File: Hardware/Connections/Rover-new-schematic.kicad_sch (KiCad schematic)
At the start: 7 parts, among them J1 Motor_Forward_Right, J2 motor_forward_left, J3 motor_back_left, J4 motor_back_right, U1 ESP32-DEVKIT-V1

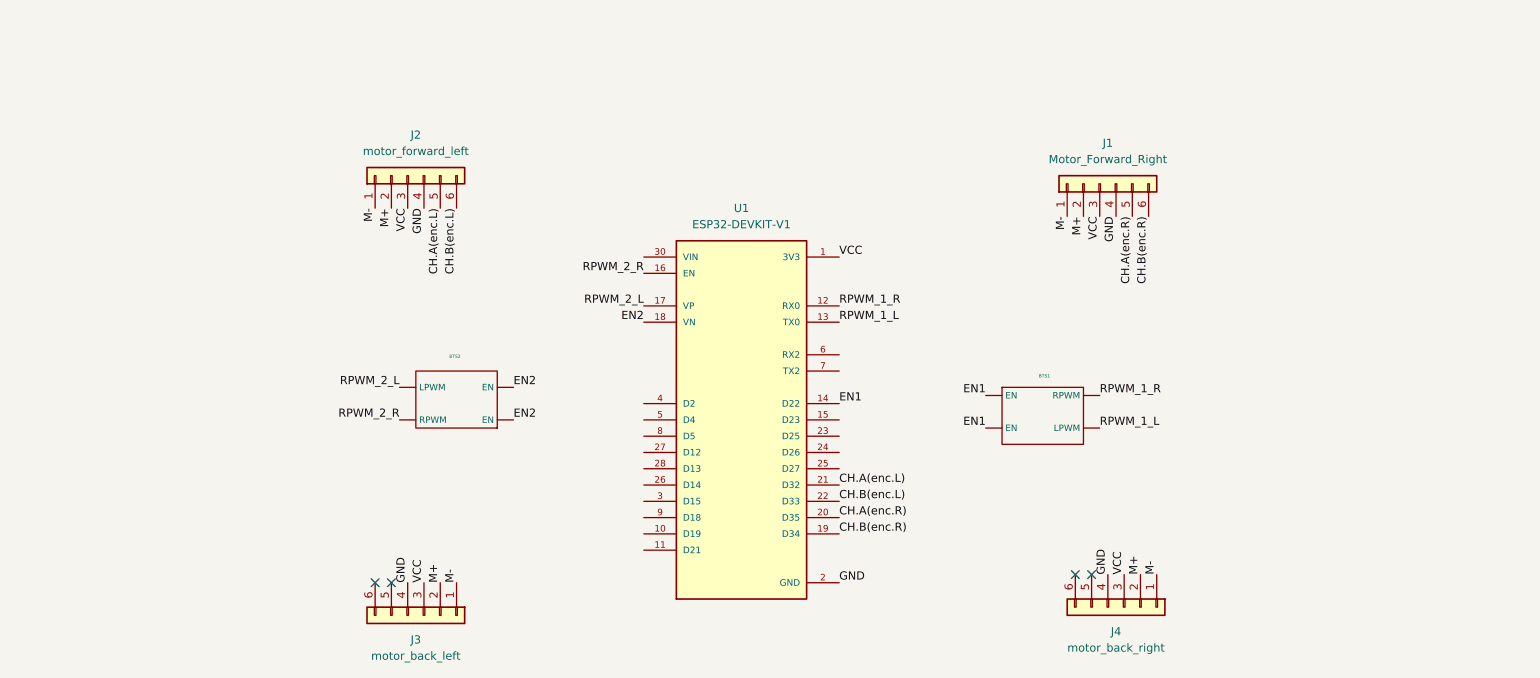
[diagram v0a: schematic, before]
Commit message: schematic modified
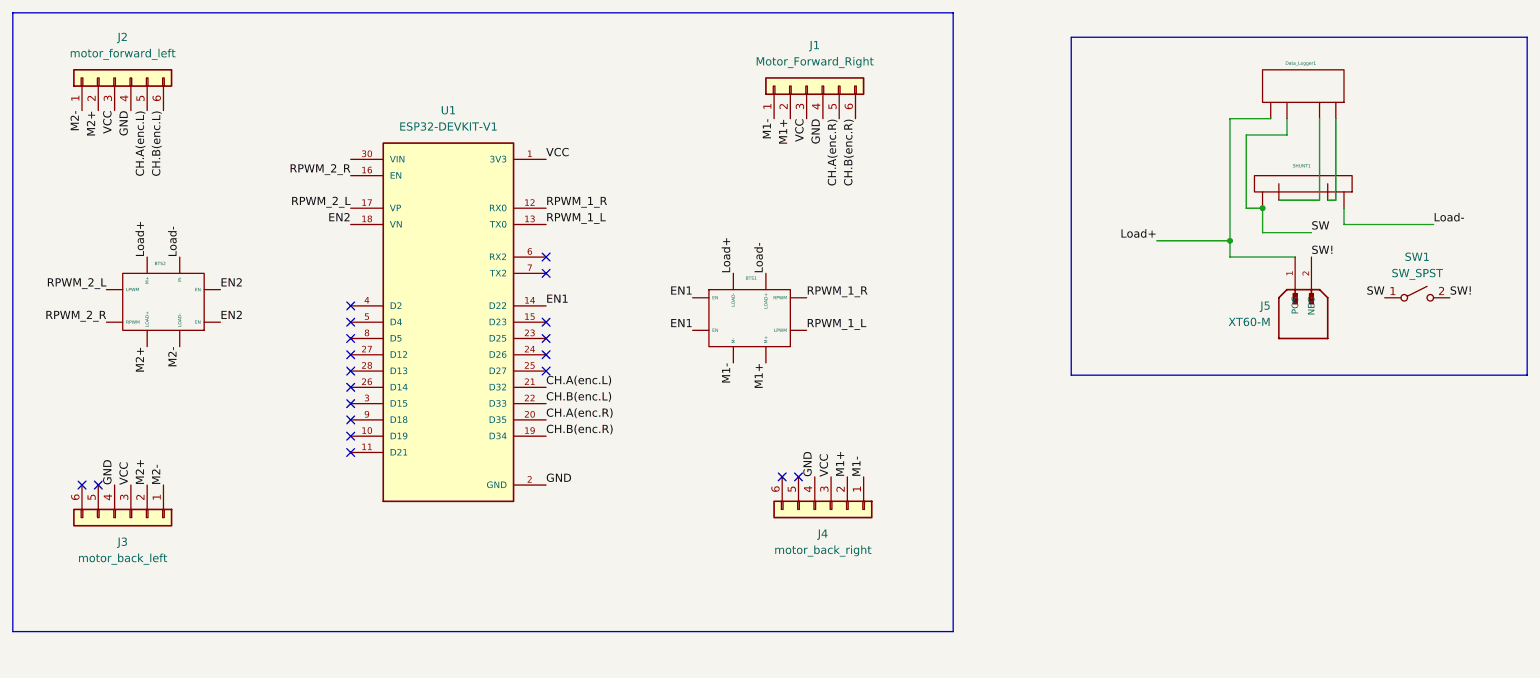
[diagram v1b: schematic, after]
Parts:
- added Data_Logger1: ~, symbol CUSTOM_DESIGNS:Data_Logger
- added J5: XT60-M, AMASS_XT60-M, symbol ROVER:XT60-M
- added SHUNT1: ~, symbol CUSTOM_DESIGNS:Logger_shunt
- added SW1: SW_SPST, symbol Switch:SW_SPST
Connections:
- net M+ renamed M1+
- net M1+: now also BTS1. (LPWM); no longer J2.2 (Pin_2), J3.2 (Pin_2)
- net M- renamed M1-
- net M1-: now also BTS1. (LPWM); no longer J2.1 (Pin_1), J3.1 (Pin_1)
- new net: Data_Logger1., SHUNT1. (x2)
- new net Load+: BTS1. (LPWM), BTS2. (LPWM), Data_Logger1., J5.1 (POS)
- new net Load-: BTS1. (LPWM), BTS2. (LPWM), SHUNT1.
- new net M2+: BTS2. (LPWM), J2.2 (Pin_2), J3.2 (Pin_2)
- new net M2-: BTS2. (LPWM), J2.1 (Pin_1), J3.1 (Pin_1)
- new net SW: Data_Logger1., SHUNT1., SW1.1 (A)
- new net SW!: J5.2 (NEG), SW1.2 (B)
- no-connect marks 4 -> 20
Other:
- moved on the sheet: J1, J2, J3, J4, U1
